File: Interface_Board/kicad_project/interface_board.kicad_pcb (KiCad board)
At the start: 2 copper layers, 58 x 37 mm, 41 parts, among them J1 INPUT, J2 Conn_01x12, J3 Conn_01x12, SW1 RESET, U1 TPS563200, U2 TPS563200, U3 PCA9600DP, U4 MCP23008SS, U5 SC18IS602B

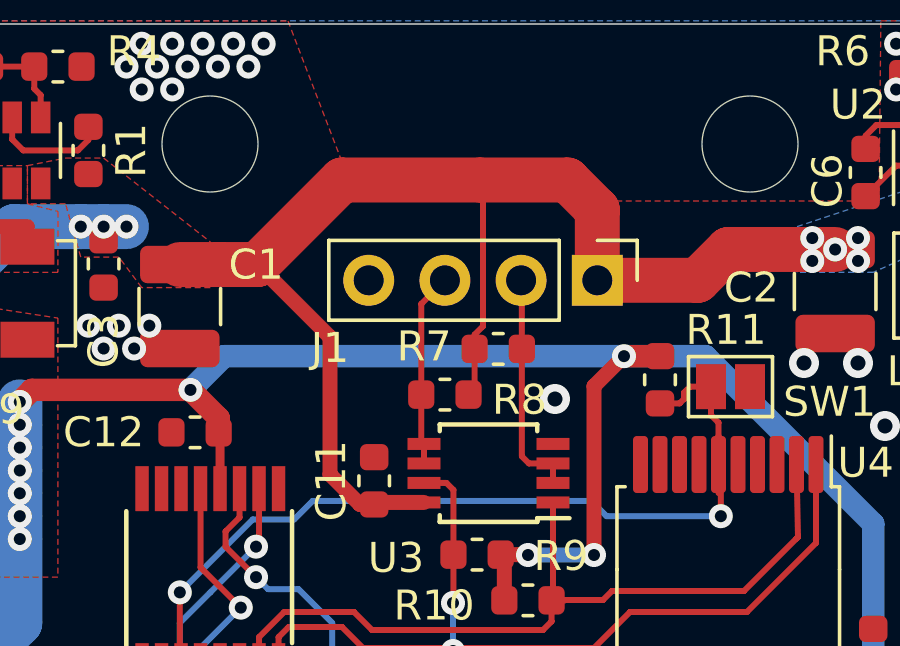
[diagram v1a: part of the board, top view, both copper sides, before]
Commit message: add input protection to interface board
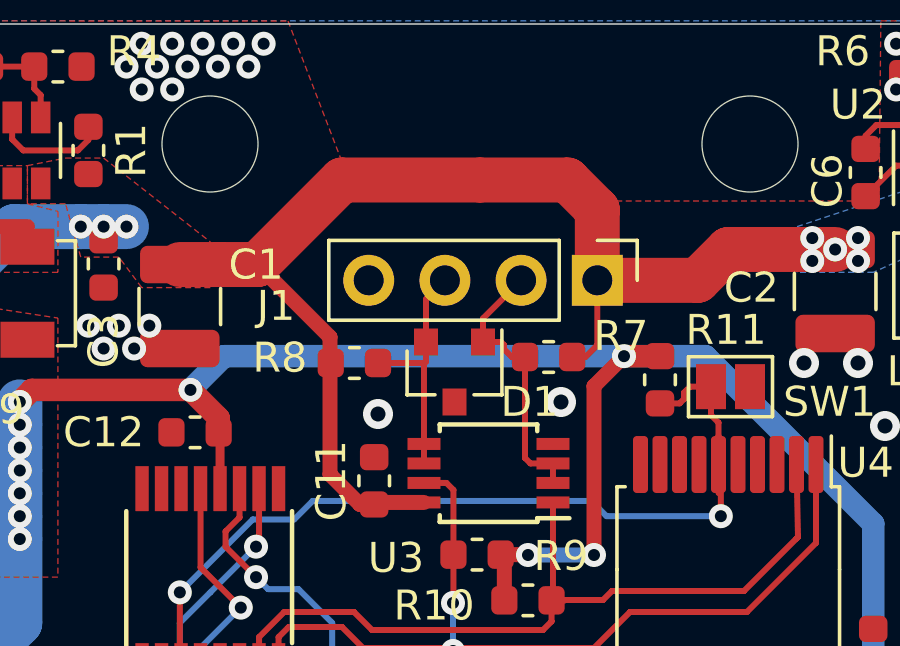
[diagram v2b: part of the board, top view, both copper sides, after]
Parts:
- added D1: PESD12VS2UT, Package_TO_SOT_SMD:SOT-23, F.Cu at (88.2, 68.6)
- moved R8 3.20 mm to (84.8, 68.3), turned to 0 degrees
- moved R7 1.70 mm to (91.3, 68.1), turned to 180 degrees
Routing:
- net +12V: track 88.9 -> 84.8 mm
- net Net-(D1-Pad2): track 6.34 -> 8.01 mm
- net Net-(D1-Pad1): track 7.63 -> 9.29 mm
- net GND: vias 47 -> 48

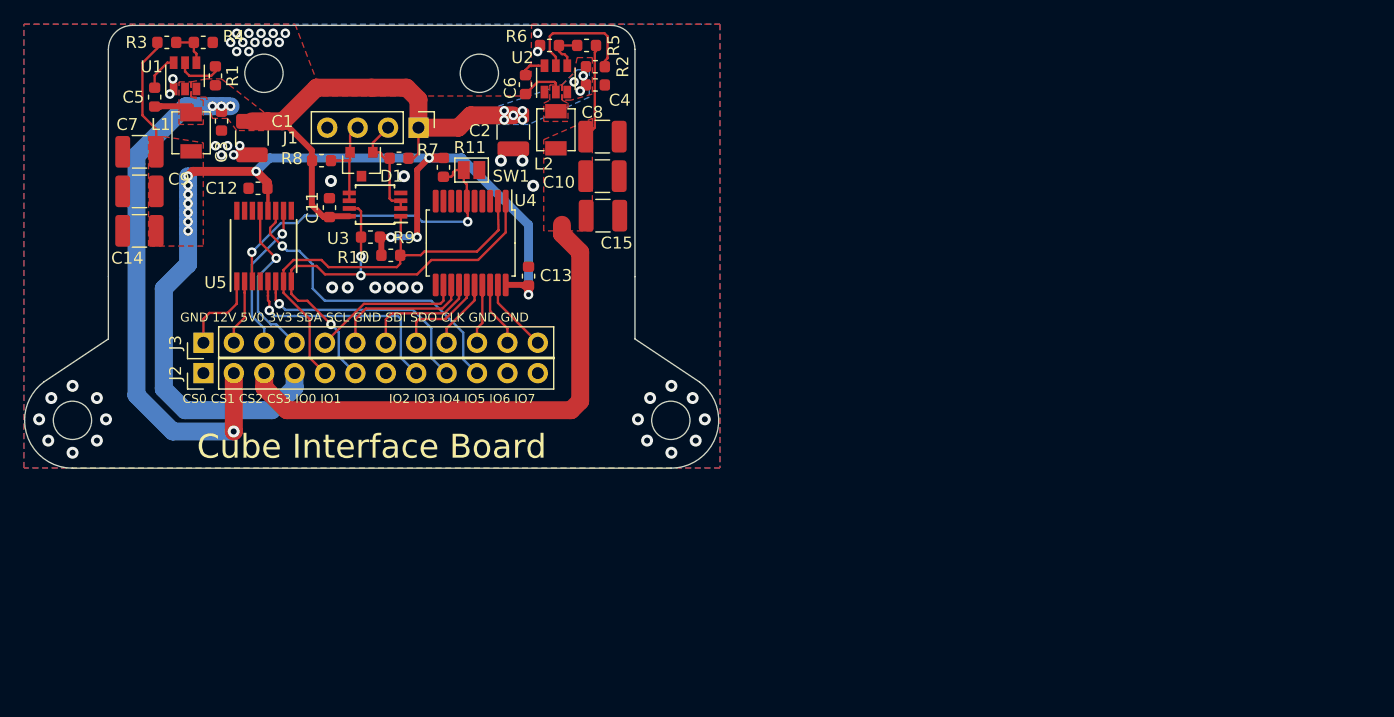
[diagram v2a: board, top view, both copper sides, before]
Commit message: interface board add new connector and edit layout
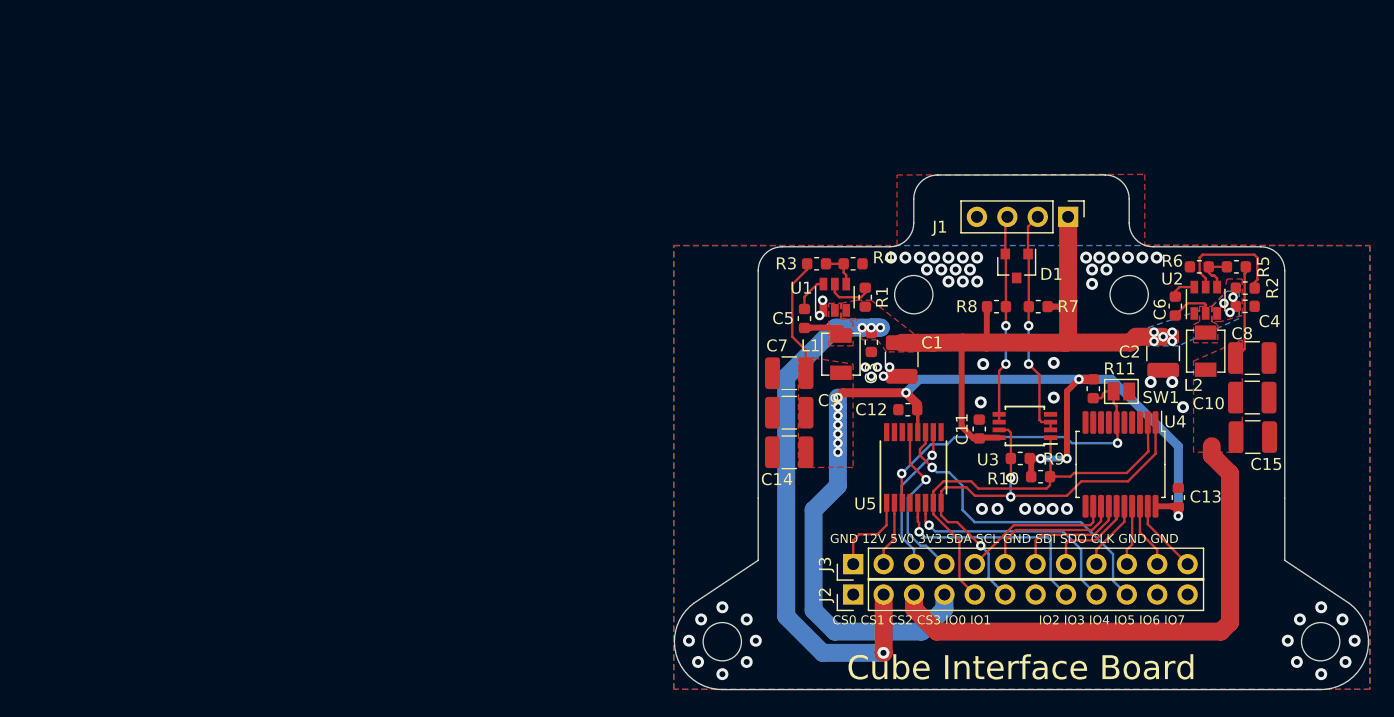
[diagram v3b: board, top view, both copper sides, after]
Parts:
- removed the REF** at (114.0, 90.0)
- removed the REF** at (64.0, 90.0)
- removed the REF** at (98.0, 61.0)
- removed the REF** at (80.0, 61.0)
- added REF**: MountingHole_3.2mm_M3_DIN965, MountingHole:MountingHole_3.2mm_M3_DIN965, F.Cu at (168.3, 108.5)
- added REF**: MountingHole_3.2mm_M3_DIN965, MountingHole:MountingHole_3.2mm_M3_DIN965, F.Cu at (118.3, 108.5)
- added REF**: MountingHole_3.2mm_M3_DIN965, MountingHole:MountingHole_3.2mm_M3_DIN965, F.Cu at (152.3, 79.5)
- added REF**: MountingHole_3.2mm_M3_DIN965, MountingHole:MountingHole_3.2mm_M3_DIN965, F.Cu at (134.3, 79.5)
- moved R8 57.7 mm to (141.2, 80.5)
- moved C1 57.4 mm to (133.3, 84.9)
- moved C2 57.4 mm to (155.1, 84.4)
- moved C4 57.4 mm to (162.0, 80.5)
- moved R1 57.4 mm to (130.2, 79.7)
- moved R10 57.4 mm to (144.9, 94.7)
- moved R11 57.4 mm to (149.3, 87.4)
- moved R2 57.4 mm to (162.0, 79.0)
- moved R6 57.4 mm to (158.2, 77.2)
- moved SW1 57.4 mm to (151.7, 87.6)
- moved C10 57.4 mm to (162.6, 88.1)
- moved C11 57.4 mm to (139.8, 90.7)
- moved C12 57.4 mm to (133.8, 89.1)
- moved C14 57.4 mm to (123.9, 92.7)
- moved C3 57.4 mm to (130.8, 83.5)
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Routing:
- net Net-(D1-Pad1): track 9.29 -> 19.4 mm, vias 0 -> 2
- net Net-(D1-Pad2): track 8.01 -> 17.5 mm, vias 0 -> 2
- net +12V: track 84.8 -> 92.6 mm
- net GND: vias 48 -> 59
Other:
- board size 58 x 37 mm -> 58 x 43 mm

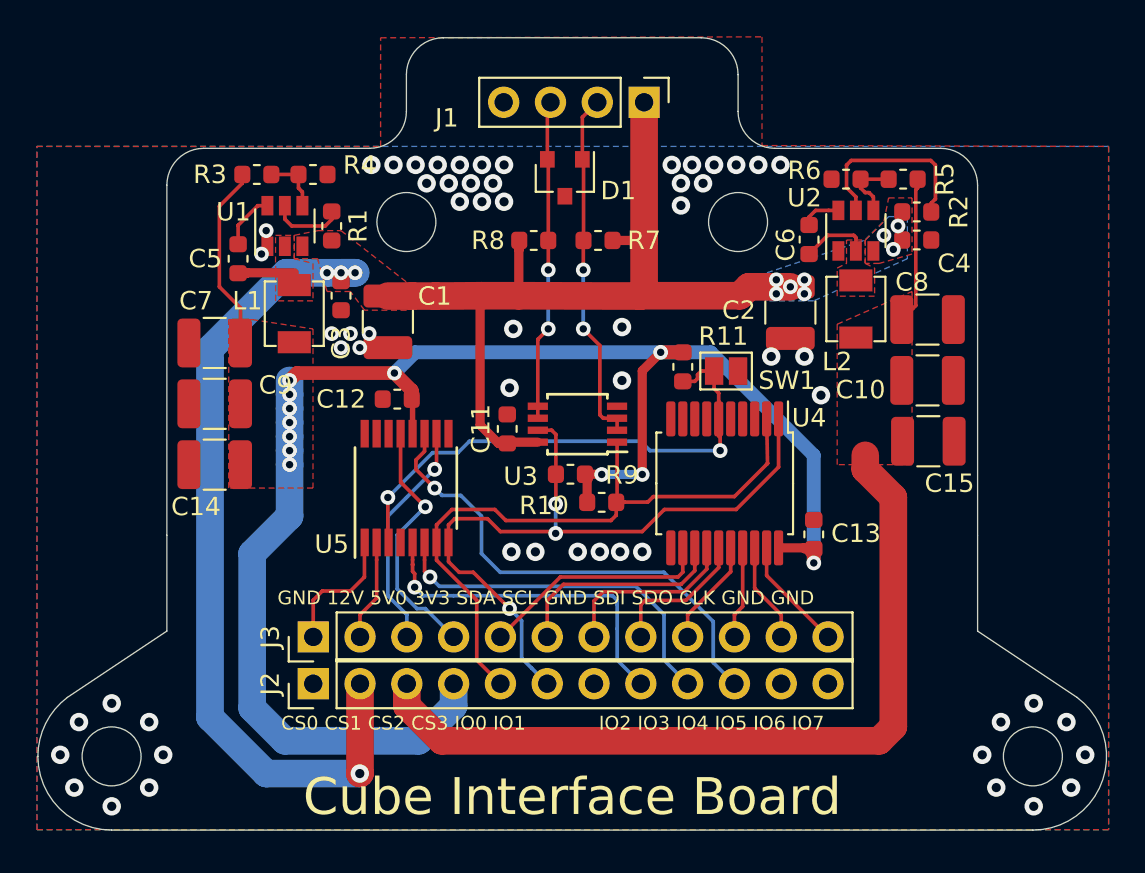
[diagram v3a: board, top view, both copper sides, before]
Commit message: change connector for interface board, edit silkscreen layers for interface and main boards
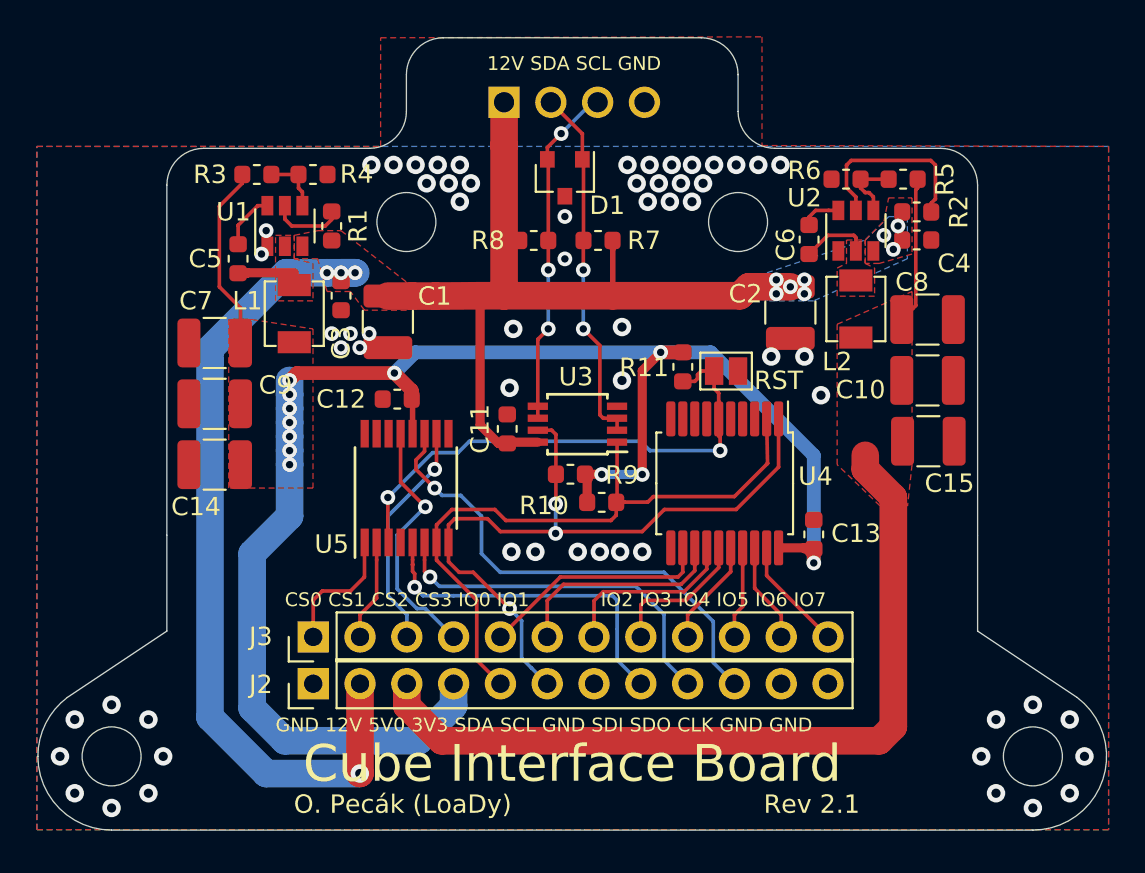
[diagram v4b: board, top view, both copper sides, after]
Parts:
- J1: footprint Connector_PinHeader_2.54mm:PinHeader_1x04_P2.54mm_Vertical -> LoaDy:Molex_70543-0003; moved to B.Cu
- moved J1 7.60 mm to (139.6, 73.0)
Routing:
- net Net-(D1-Pad2): track 17.5 -> 18.7 mm, vias 2 -> 3
- net +12V: track 92.6 -> 91.6 mm
- net Net-(D1-Pad1): track 19.4 -> 20.0 mm
- net GND: vias 59 -> 62
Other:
- board text added: "12V SDA SCL GND"
- board text added: "O. Pecák (LoaDy)"
- board text added: "RST"
- board text added: "Rev 2.1"

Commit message: add interface board silkscreen, modify main board silkscreen
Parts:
- added G***: LOGO, kicad_project:logo_cube, B.Cu at (148.0, 89.3)
- added REF**: OSHW-Symbol_6.7x6mm_SilkScreen, Symbol:OSHW-Symbol_6.7x6mm_SilkScreen, B.Cu at (131.8, 108.9)
- added REF**: KiCad-Logo2_5mm_SilkScreen, Symbol:KiCad-Logo2_5mm_SilkScreen, B.Cu at (156.9, 97.6)
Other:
- board text added: "Designed and used in EmLab at MUNI FI"
- board text added: "Github and Twitter: LoaDy588"
- board text added: "Licensed under CERN-OHL-W v2"
- board text added: "Repo: github.com/LoaDy588/cube_electronics"
